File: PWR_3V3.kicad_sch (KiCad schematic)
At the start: 12 parts, among them IC2 TPS628101HQWRWYRQ1

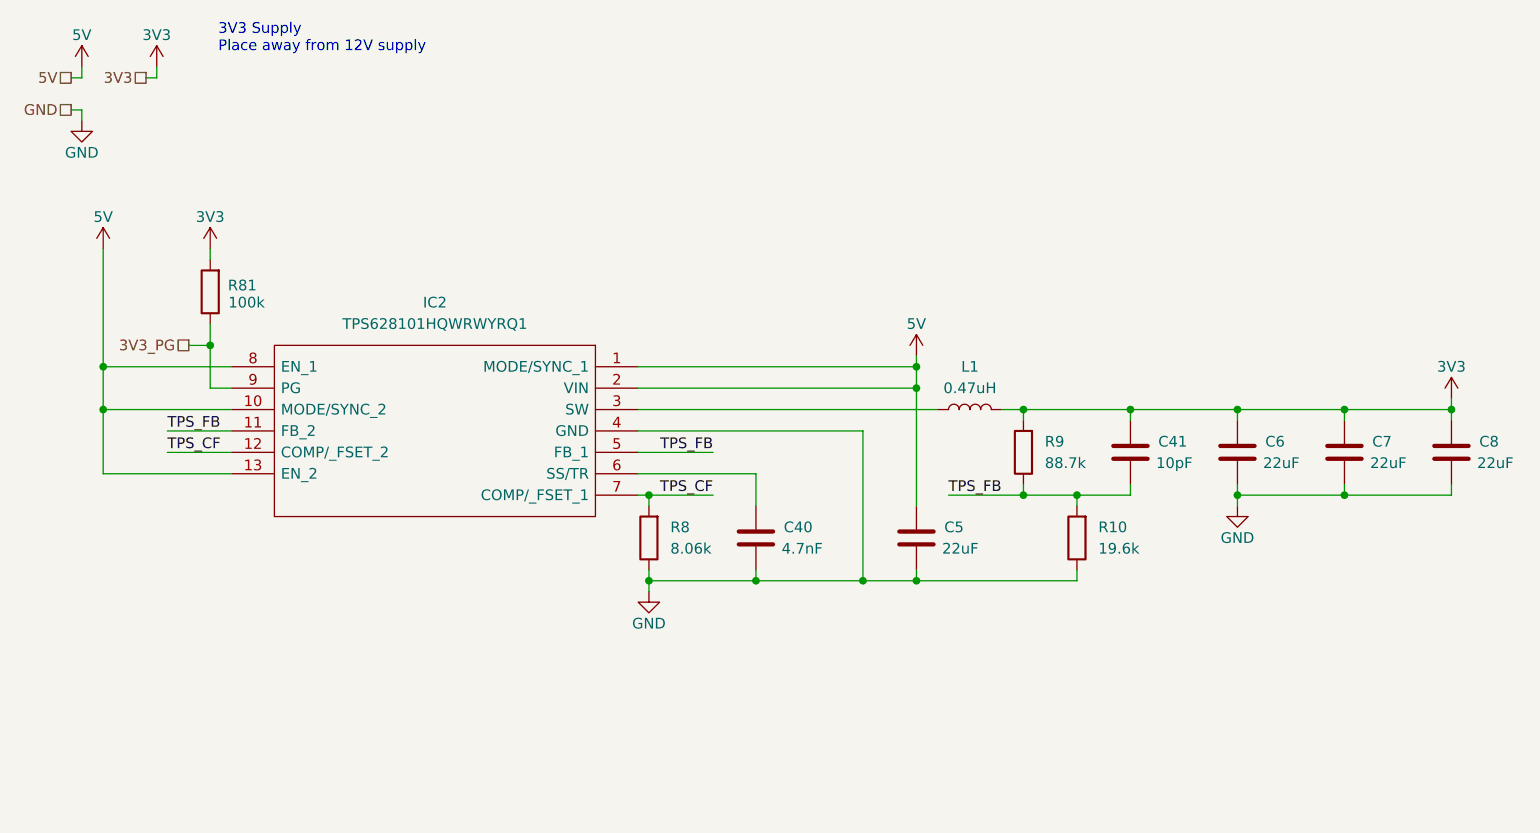
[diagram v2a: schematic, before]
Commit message: finished initial esp routing
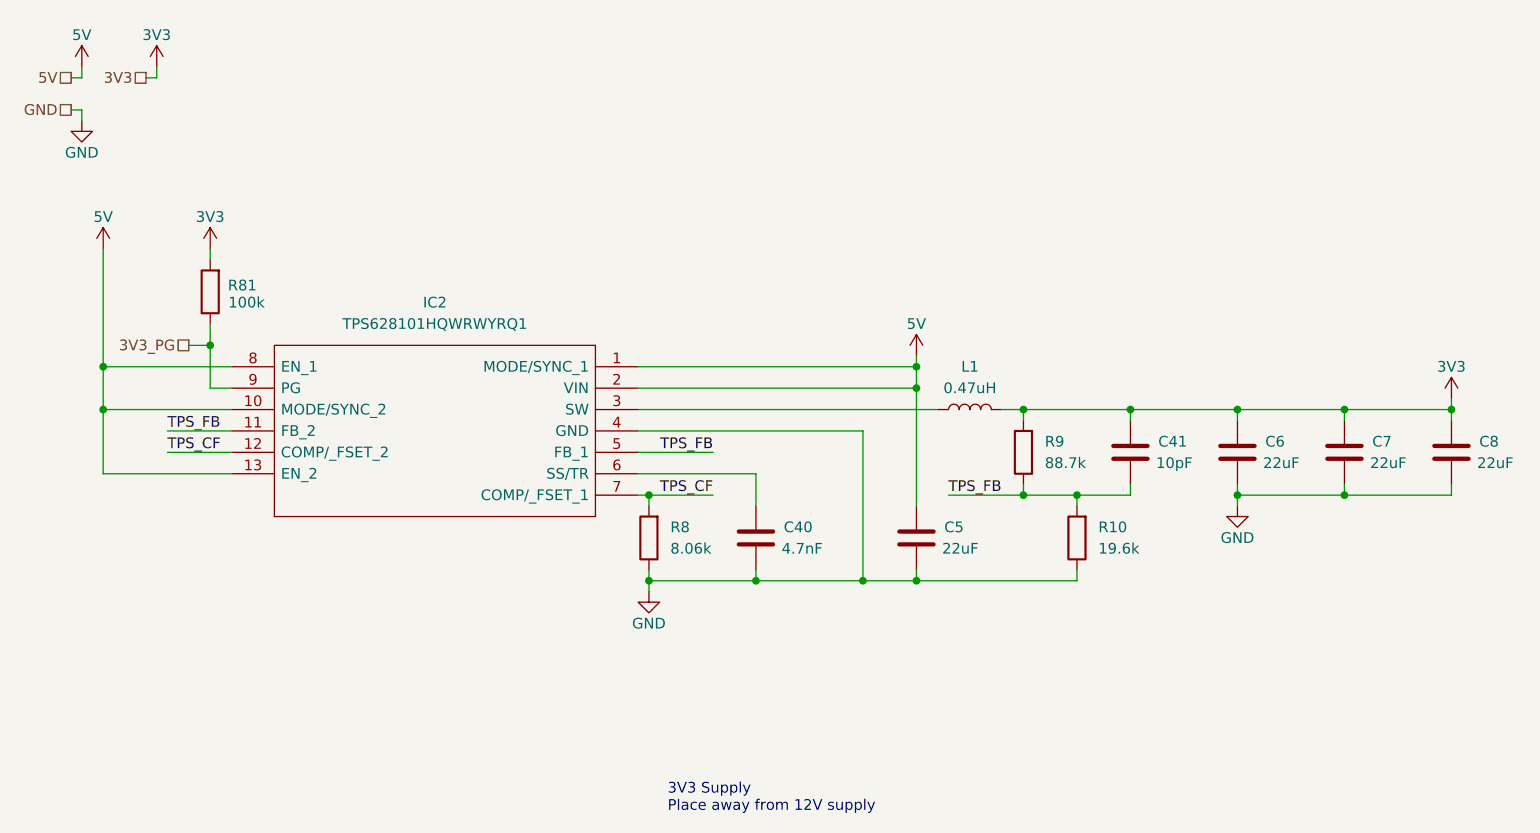
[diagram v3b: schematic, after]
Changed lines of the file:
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@@
 	(text_box "3V3 Supply\nPlace away from 12V supply"
 		(exclude_from_sim no)
-		(at 36.83 13.97 0)
+		(at 90.17 104.14 0)
 		(size 30.48 6.35)
 		(margins 0.9525 0.9525 0.9525 0.9525)

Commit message: redid annotations, added test point
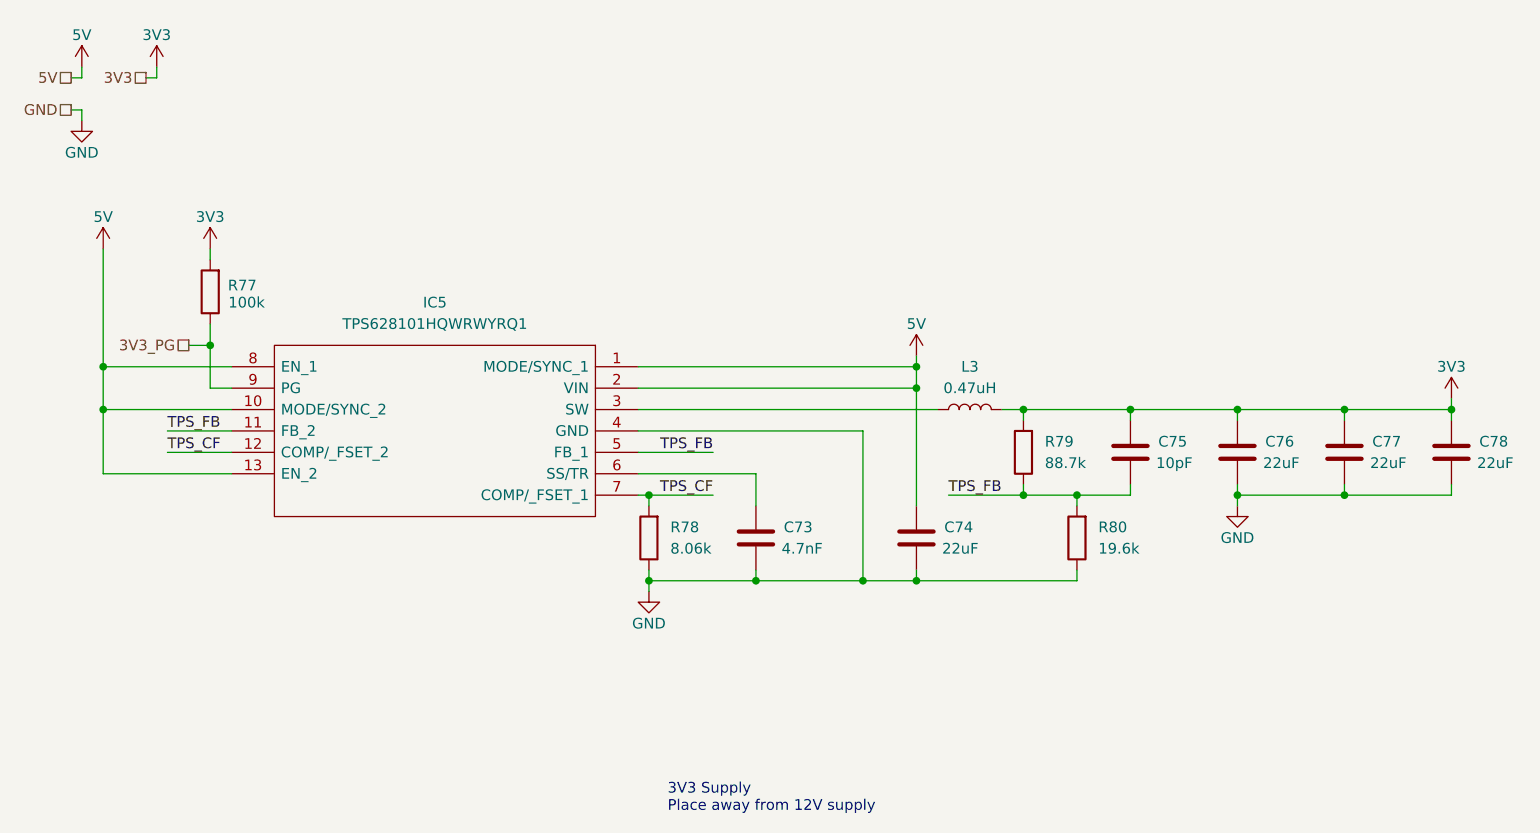
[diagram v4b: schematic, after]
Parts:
- renumbered C40 to C73, C5 to C74, C41 to C75, C6 to C76, C7 to C77, C8 to C78, IC2 to IC5, L1 to L3, R81 to R77, R8 to R78, R9 to R79, R10 to R80
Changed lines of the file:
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@@
 		(dnp no)
 		(fields_autoplaced yes)
-		(property "Reference" "R10"
+		(property "Reference" "R80"
 			(at 142.24 74.9299 0)
 			(effects
@@
 			(project "NCU"
 				(path "/3aee14c3-5480-4f7c-989e-3fef81779034/05e3be97-98f6-4518-a1a7-240d4da327e6/c5136008-5582-44d5-9c96-36b624677ffa"
-					(reference "R10")
+					(reference "R80")
 					(unit 1)
 				)
@@
 		(on_board yes)
 		(dnp no)
-		(property "Reference" "R81"
+		(property "Reference" "R77"
 			(at 40.64 46.228 0)
 			(effects
@@
 			(project "NCU"
 				(path "/3aee14c3-5480-4f7c-989e-3fef81779034/05e3be97-98f6-4518-a1a7-240d4da327e6/c5136008-5582-44d5-9c96-36b624677ffa"
-					(reference "R81")
+					(reference "R77")
 					(unit 1)
 				)
@@
 		(on_board yes)
 		(dnp no)
-		(property "Reference" "#PWR0269"
+		(property "Reference" "#PWR0276"
 			(at 21.59 33.02 0)
 			(effects
@@
 			(project "NCU"
 				(path "/3aee14c3-5480-4f7c-989e-3fef81779034/05e3be97-98f6-4518-a1a7-240d4da327e6/c5136008-5582-44d5-9c96-36b624677ffa"
-					(reference "#PWR0269")
+					(reference "#PWR0276")
 					(unit 1)
 				)
@@
 		(on_board yes)
 		(dnp no)
-		(property "Reference" "#PWR063"
+		(property "Reference" "#PWR0280"
 			(at 88.9 88.9 0)
 			(effects
@@
 			(project "NCU"
 				(path "/3aee14c3-5480-4f7c-989e-3fef81779034/05e3be97-98f6-4518-a1a7-240d4da327e6/c5136008-5582-44d5-9c96-36b624677ffa"
-					(reference "#PWR063")
+					(reference "#PWR0280")
 					(unit 1)
 				)
@@
 		(on_board yes)
 		(dnp no)
-		(property "Reference" "#PWR061"
+		(property "Reference" "#PWR0283"
 			(at 184.15 63.5 0)
 			(effects
@@
 			(project "NCU"
 				(path "/3aee14c3-5480-4f7c-989e-3fef81779034/05e3be97-98f6-4518-a1a7-240d4da327e6/c5136008-5582-44d5-9c96-36b624677ffa"
-					(reference "#PWR061")
+					(reference "#PWR0283")
 					(unit 1)
 				)
@@
 		(on_board yes)
 		(dnp no)
-		(property "Reference" "#PWR058"
+		(property "Reference" "#PWR0277"
 			(at 24.13 45.72 0)
 			(effects
@@
 			(project "NCU"
 				(path "/3aee14c3-5480-4f7c-989e-3fef81779034/05e3be97-98f6-4518-a1a7-240d4da327e6/c5136008-5582-44d5-9c96-36b624677ffa"
-					(reference "#PWR058")
+					(reference "#PWR0277")
 					(unit 1)
 				)
@@
 		(dnp no)
 		(fields_autoplaced yes)
-		(property "Reference" "R8"
+		(property "Reference" "R78"
 			(at 91.44 74.9299 0)
 			(effects
@@
 			(project "NCU"
 				(path "/3aee14c3-5480-4f7c-989e-3fef81779034/05e3be97-98f6-4518-a1a7-240d4da327e6/c5136008-5582-44d5-9c96-36b624677ffa"
-					(reference "R8")
+					(reference "R78")
 					(unit 1)
 				)
@@
 		(on_board yes)
 		(dnp no)
-		(property "Reference" "C8"
+		(property "Reference" "C78"
 			(at 187.452 64.77 0)
 			(effects
@@
 			(project "NCU"
 				(path "/3aee14c3-5480-4f7c-989e-3fef81779034/05e3be97-98f6-4518-a1a7-240d4da327e6/c5136008-5582-44d5-9c96-36b624677ffa"
-					(reference "C8")
+					(reference "C78")
 					(unit 1)
 				)
@@
 		(on_board yes)
 		(dnp no)
-		(property "Reference" "#PWR062"
+		(property "Reference" "#PWR0282"
 			(at 158.75 78.74 0)
 			(effects
@@
 			(project "NCU"
 				(path "/3aee14c3-5480-4f7c-989e-3fef81779034/05e3be97-98f6-4518-a1a7-240d4da327e6/c5136008-5582-44d5-9c96-36b624677ffa"
-					(reference "#PWR062")
+					(reference "#PWR0282")
 					(unit 1)
 				)
@@
 		(dnp no)
 		(fields_autoplaced yes)
-		(property "Reference" "L1"
+		(property "Reference" "L3"
 			(at 127 55.88 90)
 			(effects
@@
 			(project "NCU"
 				(path "/3aee14c3-5480-4f7c-989e-3fef81779034/05e3be97-98f6-4518-a1a7-240d4da327e6/c5136008-5582-44d5-9c96-36b624677ffa"
-					(reference "L1")
+					(reference "L3")
 					(unit 1)
 				)
@@
 		(on_board yes)
 		(dnp no)
-		(property "Reference" "C7"
+		(property "Reference" "C77"
 			(at 174.752 64.77 0)
 			(effects
@@
 			(project "NCU"
 				(path "/3aee14c3-5480-4f7c-989e-3fef81779034/05e3be97-98f6-4518-a1a7-240d4da327e6/c5136008-5582-44d5-9c96-36b624677ffa"
-					(reference "C7")
+					(reference "C77")
 					(unit 1)
 				)
@@
 		(on_board yes)
 		(dnp no)
-		(property "Reference" "#PWR0272"
+		(property "Reference" "#PWR0278"
 			(at 30.48 24.13 0)
 			(effects
@@
 			(project "NCU"
 				(path "/3aee14c3-5480-4f7c-989e-3fef81779034/05e3be97-98f6-4518-a1a7-240d4da327e6/c5136008-5582-44d5-9c96-36b624677ffa"
-					(reference "#PWR0272")
+					(reference "#PWR0278")
 					(unit 1)
 				)
@@
 		(dnp no)
 		(fields_autoplaced yes)
-		(property "Reference" "IC2"
+		(property "Reference" "IC5"
 			(at 63.5 48.26 0)
 			(effects
@@
 			(project "NCU"
 				(path "/3aee14c3-5480-4f7c-989e-3fef81779034/05e3be97-98f6-4518-a1a7-240d4da327e6/c5136008-5582-44d5-9c96-36b624677ffa"
-					(reference "IC2")
+					(reference "IC5")
 					(unit 1)
 				)
@@
 		(dnp no)
 		(fields_autoplaced yes)
-		(property "Reference" "R9"
+		(property "Reference" "R79"
 			(at 135.89 64.7699 0)
 			(effects
@@
 			(project "NCU"
 				(path "/3aee14c3-5480-4f7c-989e-3fef81779034/05e3be97-98f6-4518-a1a7-240d4da327e6/c5136008-5582-44d5-9c96-36b624677ffa"
-					(reference "R9")
+					(reference "R79")
 					(unit 1)
 				)
@@
 		(on_board yes)
 		(dnp no)
-		(property "Reference" "#PWR060"
+		(property "Reference" "#PWR0281"
 			(at 120.65 58.42 0)
 			(effects
@@
 			(project "NCU"
 				(path "/3aee14c3-5480-4f7c-989e-3fef81779034/05e3be97-98f6-4518-a1a7-240d4da327e6/c5136008-5582-44d5-9c96-36b624677ffa"
-					(reference "#PWR060")
+					(reference "#PWR0281")
 					(unit 1)
 				)
@@
 		(on_board yes)
 		(dnp no)
-		(property "Reference" "#PWR0270"
+		(property "Reference" "#PWR0275"
 			(at 21.59 24.13 0)
 			(effects
@@
 			(project "NCU"
 				(path "/3aee14c3-5480-4f7c-989e-3fef81779034/05e3be97-98f6-4518-a1a7-240d4da327e6/c5136008-5582-44d5-9c96-36b624677ffa"
-					(reference "#PWR0270")
+					(reference "#PWR0275")
 					(unit 1)
 				)
@@
 		(on_board yes)
 		(dnp no)
-		(property "Reference" "C41"
+		(property "Reference" "C75"
 			(at 149.352 64.77 0)
 			(effects
@@
 			(project "NCU"
 				(path "/3aee14c3-5480-4f7c-989e-3fef81779034/05e3be97-98f6-4518-a1a7-240d4da327e6/c5136008-5582-44d5-9c96-36b624677ffa"
-					(reference "C41")
+					(reference "C75")
 					(unit 1)
 				)
@@
 		(on_board yes)
 		(dnp no)
-		(property "Reference" "C5"
+		(property "Reference" "C74"
 			(at 123.952 74.93 0)
 			(effects
@@
 			(project "NCU"
 				(path "/3aee14c3-5480-4f7c-989e-3fef81779034/05e3be97-98f6-4518-a1a7-240d4da327e6/c5136008-5582-44d5-9c96-36b624677ffa"
-					(reference "C5")
+					(reference "C74")
 					(unit 1)
 				)
@@
 		(on_board yes)
 		(dnp no)
-		(property "Reference" "C40"
+		(property "Reference" "C73"
 			(at 104.902 74.93 0)
 			(effects
@@
 			(project "NCU"
 				(path "/3aee14c3-5480-4f7c-989e-3fef81779034/05e3be97-98f6-4518-a1a7-240d4da327e6/c5136008-5582-44d5-9c96-36b624677ffa"
-					(reference "C40")
+					(reference "C73")
 					(unit 1)
 				)
@@
 		(on_board yes)
 		(dnp no)
-		(property "Reference" "#PWR0265"
+		(property "Reference" "#PWR0279"
 			(at 36.83 45.72 0)
 			(effects
@@
 			(project "NCU"
 				(path "/3aee14c3-5480-4f7c-989e-3fef81779034/05e3be97-98f6-4518-a1a7-240d4da327e6/c5136008-5582-44d5-9c96-36b624677ffa"
-					(reference "#PWR0265")
+					(reference "#PWR0279")
 					(unit 1)
 				)
@@
 		(on_board yes)
 		(dnp no)
-		(property "Reference" "C6"
+		(property "Reference" "C76"
 			(at 162.052 64.77 0)
 			(effects
@@
 			(project "NCU"
 				(path "/3aee14c3-5480-4f7c-989e-3fef81779034/05e3be97-98f6-4518-a1a7-240d4da327e6/c5136008-5582-44d5-9c96-36b624677ffa"
-					(reference "C6")
-					(unit 1)
-				)
+					(reference "C76")
+					(unit 1)
+				)
